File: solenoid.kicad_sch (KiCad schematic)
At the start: 10 parts, among them J9 Solenoid, Q8 DMG3402L

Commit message: Updated schematic. No filtering but besides that finished. Need to fix footprints and start layout.
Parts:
- J9: footprint TerminalBlock:TerminalBlock_bornier-3_P5.08mm -> 0UCIRP-KiCAD-Lib:GX-16 3 pin
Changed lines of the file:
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@@
 			)
 		)
-		(property "Footprint" "TerminalBlock:TerminalBlock_bornier-3_P5.08mm"
+		(property "Footprint" "0UCIRP-KiCAD-Lib:GX-16 3 pin"
 			(at 109.22 83.82 0)
 			(effects

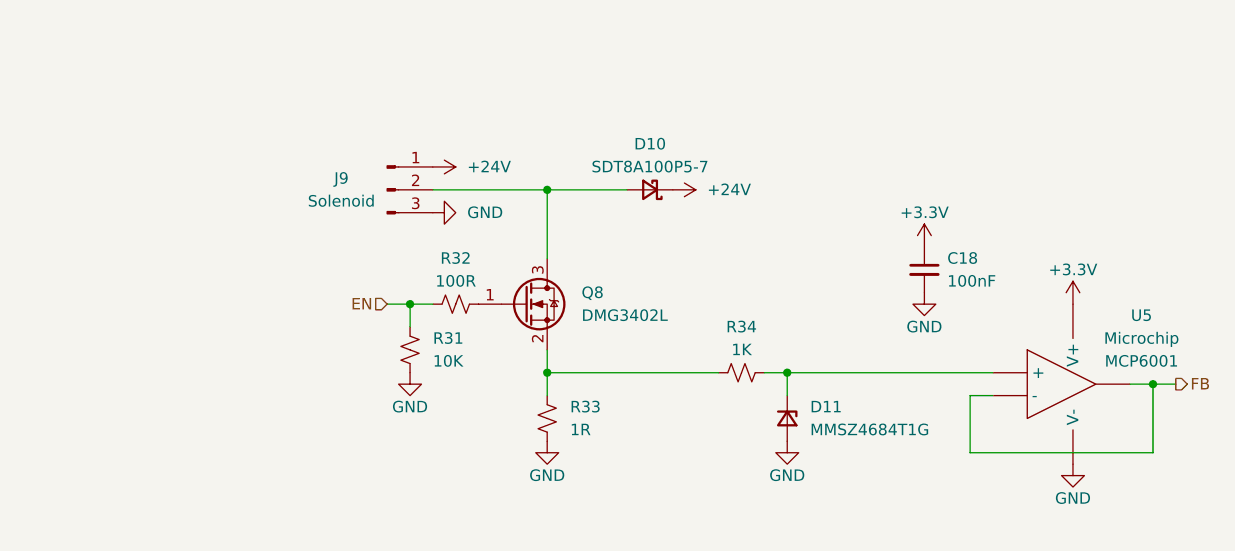
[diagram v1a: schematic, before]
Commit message: Added LC filter for power filtering
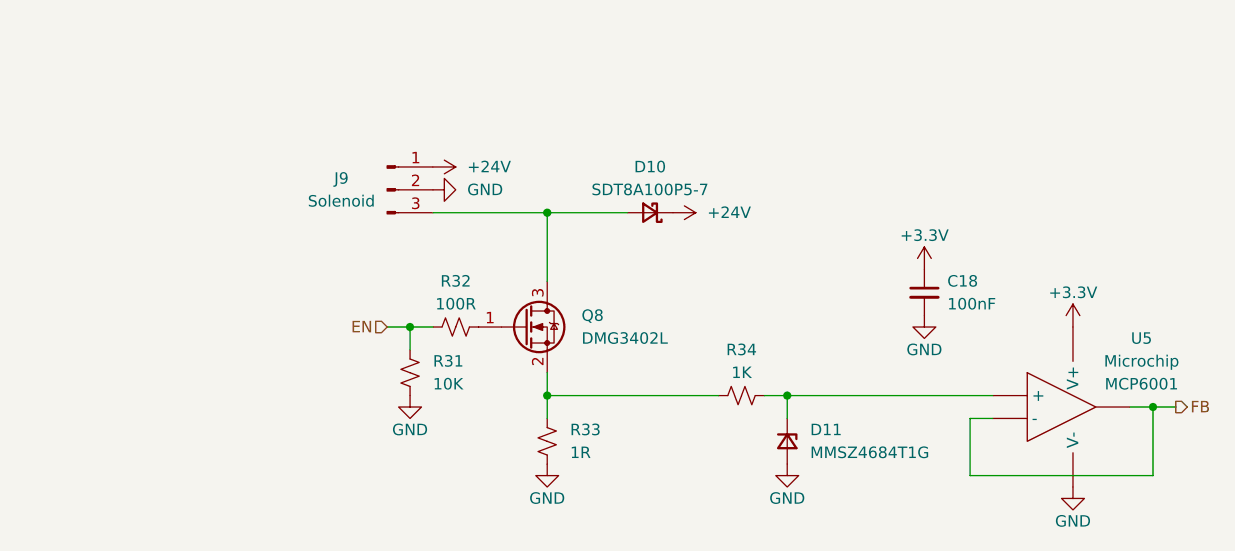
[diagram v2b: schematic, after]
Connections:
- net GND: now also J9.2 (Pin_2); no longer J9.3 (Pin_3)
- net at D10.2 (A), Q8.3 (D): now also J9.3 (Pin_3); no longer J9.2 (Pin_2)
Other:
- moved on the sheet: C18, D10, D11, Q8, R31, R32, R33, R34, U5

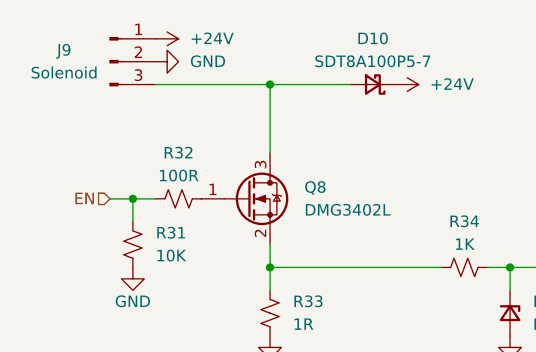
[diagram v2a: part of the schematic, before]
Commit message: Updated kicad lib commit, maybe correct now
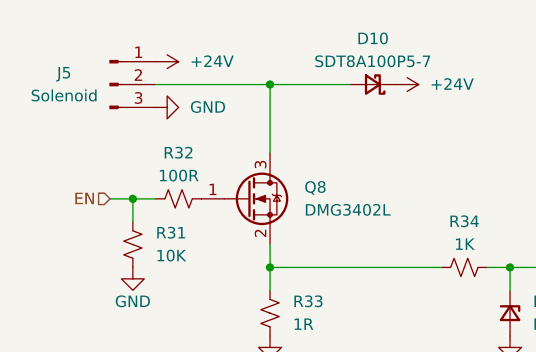
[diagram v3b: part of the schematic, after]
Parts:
- removed J9: Solenoid, 0UCIRP-KiCAD-Lib:GX-16 3 pin, symbol Connector:Conn_01x03_Pin
- added J5: Solenoid, 0UCIRP-KiCAD-Lib:GX-16 3 pin, symbol Connector:Conn_01x03_Pin
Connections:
- net +24V: now also J5.1 (Pin_1)
- net GND: now also J5.3 (Pin_3)
- net at D10.2 (A), Q8.3 (D): now also J5.2 (Pin_2)
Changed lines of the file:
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@@
 	(symbol
 		(lib_id "power:GND")
-		(at 114.3 83.82 90)
+		(at 114.3 88.9 90)
 		(unit 1)
 		(exclude_from_sim no)
@@
 		(fields_autoplaced yes)
 		(property "Reference" "#PWR079"
-			(at 120.65 83.82 0)
+			(at 120.65 88.9 0)
 			(effects
 				(font
@@
 		)
 		(property "Value" "GND"
-			(at 118.11 83.82 90)
+			(at 118.11 88.9 90)
 			(effects
 				(font
@@
 		)
 		(property "Footprint" ""
-			(at 114.3 83.82 0)
+			(at 114.3 88.9 0)
 			(effects
 				(font
@@
 		)
 		(property "Datasheet" ""
-			(at 114.3 83.82 0)
+			(at 114.3 88.9 0)
 			(effects
 				(font
@@
 		)
 		(property "Description" ""
-			(at 114.3 83.82 0)
+			(at 114.3 88.9 0)
 			(effects
 				(font
@@
 			(project "gse2-hardware"
 				(path "/1eb2a3ff-e0fd-4343-8dba-716780a4d459/03932ad1-129b-4688-9d97-fd8248728dfb"
-					(reference "#PWR028")
+					(reference "#PWR0103")
 					(unit 1)
 				)
 				(path "/1eb2a3ff-e0fd-4343-8dba-716780a4d459/286b6f9d-06b9-4eca-96aa-fac563af00a8"
-					(reference "#PWR063")
+					(reference "#PWR0123")
 					(unit 1)
 				)
 				(path "/1eb2a3ff-e0fd-4343-8dba-716780a4d459/3c07b789-4554-4158-a611-d22d74095257"
-					(reference "#PWR0123")
+					(reference "#PWR0429")
 					(unit 1)
 				)
@@
 				)
 				(path "/1eb2a3ff-e0fd-4343-8dba-716780a4d459/4a437018-65cd-45b6-9348-2044032dd86a"
+					(reference "#PWR0427")
+					(unit 1)
+				)
+				(path "/1eb2a3ff-e0fd-4343-8dba-716780a4d459/62945beb-192a-4537-9ce7-3a53d30b8410"
+					(reference "#PWR0421")
+					(unit 1)
+				)
+				(path "/1eb2a3ff-e0fd-4343-8dba-716780a4d459/8a44b462-584f-4ea8-be91-d4caf81deda4"
+					(reference "#PWR0425")
+					(unit 1)
+				)
+				(path "/1eb2a3ff-e0fd-4343-8dba-716780a4d459/94c0f81a-efb8-4875-8214-c5f2a6a703c9"
+					(reference "#PWR0423")
+					(unit 1)
+				)
+				(path "/1eb2a3ff-e0fd-4343-8dba-716780a4d459/dedc65d9-5cd8-484a-8156-18d824848e23"
 					(reference "#PWR0113")
-					(unit 1)
-				)
-				(path "/1eb2a3ff-e0fd-4343-8dba-716780a4d459/62945beb-192a-4537-9ce7-3a53d30b8410"
-					(reference "#PWR073")
-					(unit 1)
-				)
-				(path "/1eb2a3ff-e0fd-4343-8dba-716780a4d459/8a44b462-584f-4ea8-be91-d4caf81deda4"
-					(reference "#PWR0103")
-					(unit 1)
-				)
-				(path "/1eb2a3ff-e0fd-4343-8dba-716780a4d459/94c0f81a-efb8-4875-8214-c5f2a6a703c9"
-					(reference "#PWR093")
-					(unit 1)
-				)
-				(path "/1eb2a3ff-e0fd-4343-8dba-716780a4d459/dedc65d9-5cd8-484a-8156-18d824848e23"
-					(reference "#PWR039")
 					(unit 1)
 				)
@@
 	(symbol
 		(lib_id "power:+24V")
-		(at 114.3 81.28 270)
+		(at 114.3 83.82 270)
 		(unit 1)
 		(exclude_from_sim no)
@@
 		(fields_autoplaced yes)
 		(property "Reference" "#PWR078"
-			(at 110.49 81.28 0)
+			(at 110.49 83.82 0)
 			(effects
 				(font
@@
 		)
 		(property "Value" "+24V"
-			(at 118.11 81.28 90)
+			(at 118.11 83.82 90)
 			(effects
 				(font
@@
 		)
 		(property "Footprint" ""
-			(at 114.3 81.28 0)
+			(at 114.3 83.82 0)
 			(effects
 				(font
@@
 		)
 		(property "Datasheet" ""
-			(at 114.3 81.28 0)
+			(at 114.3 83.82 0)
 			(effects
 				(font
@@
 		)
 		(property "Description" ""
-			(at 114.3 81.28 0)
+			(at 114.3 83.82 0)
 			(effects
 				(font
@@
 			(project "gse2-hardware"
 				(path "/1eb2a3ff-e0fd-4343-8dba-716780a4d459/03932ad1-129b-4688-9d97-fd8248728dfb"
-					(reference "#PWR027")
+					(reference "#PWR0102")
 					(unit 1)
 				)
 				(path "/1eb2a3ff-e0fd-4343-8dba-716780a4d459/286b6f9d-06b9-4eca-96aa-fac563af00a8"
-					(reference "#PWR058")
+					(reference "#PWR0122")
 					(unit 1)
 				)
 				(path "/1eb2a3ff-e0fd-4343-8dba-716780a4d459/3c07b789-4554-4158-a611-d22d74095257"
-					(reference "#PWR0122")
+					(reference "#PWR0428")
 					(unit 1)
 				)
@@
 				)
 				(path "/1eb2a3ff-e0fd-4343-8dba-716780a4d459/4a437018-65cd-45b6-9348-2044032dd86a"
+					(reference "#PWR0426")
+					(unit 1)
+				)
+				(path "/1eb2a3ff-e0fd-4343-8dba-716780a4d459/62945beb-192a-4537-9ce7-3a53d30b8410"
+					(reference "#PWR0420")
+					(unit 1)
+				)
+				(path "/1eb2a3ff-e0fd-4343-8dba-716780a4d459/8a44b462-584f-4ea8-be91-d4caf81deda4"
+					(reference "#PWR0424")
+					(unit 1)
+				)
+				(path "/1eb2a3ff-e0fd-4343-8dba-716780a4d459/94c0f81a-efb8-4875-8214-c5f2a6a703c9"
+					(reference "#PWR0422")
+					(unit 1)
+				)
+				(path "/1eb2a3ff-e0fd-4343-8dba-716780a4d459/dedc65d9-5cd8-484a-8156-18d824848e23"
 					(reference "#PWR0112")
-					(unit 1)
-				)
-				(path "/1eb2a3ff-e0fd-4343-8dba-716780a4d459/62945beb-192a-4537-9ce7-3a53d30b8410"
-					(reference "#PWR072")
-					(unit 1)
-				)
-				(path "/1eb2a3ff-e0fd-4343-8dba-716780a4d459/8a44b462-584f-4ea8-be91-d4caf81deda4"
-					(reference "#PWR0102")
-					(unit 1)
-				)
-				(path "/1eb2a3ff-e0fd-4343-8dba-716780a4d459/94c0f81a-efb8-4875-8214-c5f2a6a703c9"
-					(reference "#PWR092")
-					(unit 1)
-				)
-				(path "/1eb2a3ff-e0fd-4343-8dba-716780a4d459/dedc65d9-5cd8-484a-8156-18d824848e23"
-					(reference "#PWR038")
-					(unit 1)
-				)
-			)
-		)
-	)
-	(symbol
-		(lib_id "Connector:Conn_01x03_Pin")
-		(at 109.22 83.82 0)
-		(unit 1)
-		(exclude_from_sim no)
-		(in_bom yes)
-		(on_board yes)
-		(dnp no)
-		(property "Reference" "J9"
-			(at 104.14 82.55 0)
-			(effects
-				(font
-					(size 1.27 1.27)
-				)
-			)
-		)
-		(property "Value" "Solenoid"
-			(at 104.14 85.09 0)
-			(effects
-				(font
-					(size 1.27 1.27)
-				)
-			)
-		)
-		(property "Footprint" "0UCIRP-KiCAD-Lib:GX-16 3 pin"
-			(at 109.22 83.82 0)
-			(effects
-				(font
-					(size 1.27 1.27)
-				)
-				(hide yes)
-			)
-		)
-		(property "Datasheet" "~"
-			(at 109.22 83.82 0)
-			(effects
-				(font
-					(size 1.27 1.27)
-				)
-				(hide yes)
-			)
-		)
-		(property "Description" ""
-			(at 109.22 83.82 0)
-			(effects
-				(font
-					(size 1.27 1.27)
-				)
-			)
-		)
-		(property "Manufacturer" "~"
-			(at 109.22 83.82 0)
-			(effects
-				(font
-					(size 1.27 1.27)
-				)
-				(hide yes)
-			)
-		)
-		(property "Part #" "~"
-			(at 109.22 83.82 0)
-			(effects
-				(font
-					(size 1.27 1.27)
-				)
-				(hide yes)
-			)
-		)
-		(pin "1"
-		)
-		(pin "2"
-		)
-		(pin "3"
-		)
-		(instances
-			(project "gse2-hardware"
-				(path "/1eb2a3ff-e0fd-4343-8dba-716780a4d459/03932ad1-129b-4688-9d97-fd8248728dfb"
-					(reference "J5")
-					(unit 1)
-				)
-				(path "/1eb2a3ff-e0fd-4343-8dba-716780a4d459/286b6f9d-06b9-4eca-96aa-fac563af00a8"
-					(reference "J7")
-					(unit 1)
-				)
-				(path "/1eb2a3ff-e0fd-4343-8dba-716780a4d459/3c07b789-4554-4158-a611-d22d74095257"
-					(reference "J13")
-					(unit 1)
-				)
-				(path "/1eb2a3ff-e0fd-4343-8dba-716780a4d459/466853be-b1ef-4aae-8a48-67d83205b6e0"
-					(reference "J9")
-					(unit 1)
-				)
-				(path "/1eb2a3ff-e0fd-4343-8dba-716780a4d459/4a437018-65cd-45b6-9348-2044032dd86a"
-					(reference "J12")
-					(unit 1)
-				)
-				(path "/1eb2a3ff-e0fd-4343-8dba-716780a4d459/62945beb-192a-4537-9ce7-3a53d30b8410"
-					(reference "J8")
-					(unit 1)
-				)
-				(path "/1eb2a3ff-e0fd-4343-8dba-716780a4d459/8a44b462-584f-4ea8-be91-d4caf81deda4"
-					(reference "J11")
-					(unit 1)
-				)
-				(path "/1eb2a3ff-e0fd-4343-8dba-716780a4d459/94c0f81a-efb8-4875-8214-c5f2a6a703c9"
-					(reference "J10")
-					(unit 1)
-				)
-				(path "/1eb2a3ff-e0fd-4343-8dba-716780a4d459/dedc65d9-5cd8-484a-8156-18d824848e23"
-					(reference "J6")
 					(unit 1)
 				)
@@
 					(unit 1)
 				)
+			)
+		)
+	)
+	(symbol
+		(lib_id "Connector:Conn_01x03_Pin")
+		(at 109.22 86.36 0)
+		(unit 1)
+		(exclude_from_sim no)
+		(in_bom yes)
+		(on_board yes)
+		(dnp no)
+		(property "Reference" "J5"
+			(at 104.14 85.09 0)
+			(effects
+				(font
+					(size 1.27 1.27)
+				)
+			)
+		)
+		(property "Value" "Solenoid"
+			(at 104.14 87.63 0)
+			(effects
+				(font
+					(size 1.27 1.27)
+				)
+			)
+		)
+		(property "Footprint" "0UCIRP-KiCAD-Lib:GX-16 3 pin"
+			(at 109.22 86.36 0)
+			(effects
+				(font
+					(size 1.27 1.27)
+				)
+				(hide yes)
+			)
+		)
+		(property "Datasheet" "~"
+			(at 109.22 86.36 0)
+			(effects
+				(font
+					(size 1.27 1.27)
+				)
+				(hide yes)
+			)
+		)
+		(property "Description" ""
+			(at 109.22 86.36 0)
+			(effects
+				(font
+					(size 1.27 1.27)
+				)
+			)
+		)
+		(property "Manufacturer" "~"
+			(at 109.22 86.36 0)
+			(effects
+				(font
+					(size 1.27 1.27)
+				)
+				(hide yes)
+			)
+		)
+		(property "Part #" "~"
+			(at 109.22 86.36 0)
+			(effects
+				(font
+					(size 1.27 1.27)
+				)
+				(hide yes)
+			)
+		)
+		(pin "1"
+		)
+		(pin "2"
+		)
+		(pin "3"
+		)
+		(instances
+			(project "gse2-hardware"
+				(path "/1eb2a3ff-e0fd-4343-8dba-716780a4d459/03932ad1-129b-4688-9d97-fd8248728dfb"
+					(reference "J6")
+					(unit 1)
+				)
+				(path "/1eb2a3ff-e0fd-4343-8dba-716780a4d459/286b6f9d-06b9-4eca-96aa-fac563af00a8"
+					(reference "J8")
+					(unit 1)
+				)
+				(path "/1eb2a3ff-e0fd-4343-8dba-716780a4d459/3c07b789-4554-4158-a611-d22d74095257"
+					(reference "J39")
+					(unit 1)
+				)
+				(path "/1eb2a3ff-e0fd-4343-8dba-716780a4d459/466853be-b1ef-4aae-8a48-67d83205b6e0"
+					(reference "J5")
+					(unit 1)
+				)
+				(path "/1eb2a3ff-e0fd-4343-8dba-716780a4d459/4a437018-65cd-45b6-9348-2044032dd86a"
+					(reference "J13")
+					(unit 1)
+				)
+				(path "/1eb2a3ff-e0fd-4343-8dba-716780a4d459/62945beb-192a-4537-9ce7-3a53d30b8410"
+					(reference "J10")
+					(unit 1)
+				)
+				(path "/1eb2a3ff-e0fd-4343-8dba-716780a4d459/8a44b462-584f-4ea8-be91-d4caf81deda4"
+					(reference "J12")
+					(unit 1)
+				)
+				(path "/1eb2a3ff-e0fd-4343-8dba-716780a4d459/94c0f81a-efb8-4875-8214-c5f2a6a703c9"
+					(reference "J11")
+					(unit 1)
+				)
+				(path "/1eb2a3ff-e0fd-4343-8dba-716780a4d459/dedc65d9-5cd8-484a-8156-18d824848e23"
+					(reference "J7")
+					(unit 1)
+				)

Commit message: Subsystem level layout done (prelim)
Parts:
- C18: footprint Capacitor_SMD:C_0402_1005Metric -> Capacitor_SMD:C_0603_1608Metric
- R31, R32, R34: footprint Resistor_SMD:R_0402_1005Metric -> Resistor_SMD:R_0603_1608Metric
- R33: footprint Resistor_SMD:R_2512_6332Metric -> Resistor_SMD:R_0603_1608Metric
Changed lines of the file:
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@@
 			)
 		)
-		(property "Footprint" "Resistor_SMD:R_2512_6332Metric"
+		(property "Footprint" "Resistor_SMD:R_0603_1608Metric"
 			(at 127 111.76 0)
 			(effects
@@
 			)
 		)
-		(property "Footprint" "Capacitor_SMD:C_0402_1005Metric"
+		(property "Footprint" "Capacitor_SMD:C_0603_1608Metric"
 			(at 168.91 95.25 0)
 			(effects
@@
 			)
 		)
-		(property "Footprint" "Resistor_SMD:R_0402_1005Metric"
+		(property "Footprint" "Resistor_SMD:R_0603_1608Metric"
 			(at 111.76 104.14 0)
 			(effects
@@
 			)
 		)
-		(property "Footprint" "Resistor_SMD:R_0402_1005Metric"
+		(property "Footprint" "Resistor_SMD:R_0603_1608Metric"
 			(at 148.59 106.68 0)
 			(effects
@@
 			)
 		)
-		(property "Footprint" "Resistor_SMD:R_0402_1005Metric"
+		(property "Footprint" "Resistor_SMD:R_0603_1608Metric"
 			(at 116.84 99.06 0)
 			(effects

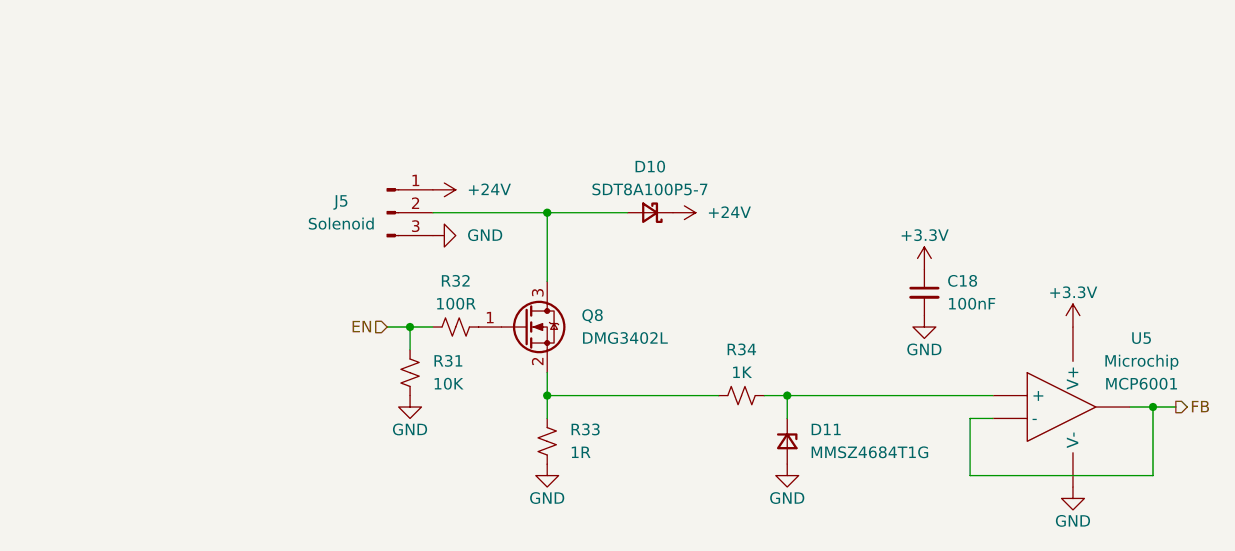
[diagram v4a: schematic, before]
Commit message: GSE v2.1: Updates for DSUB connectors for schematic only done. Layout needs a ton of work
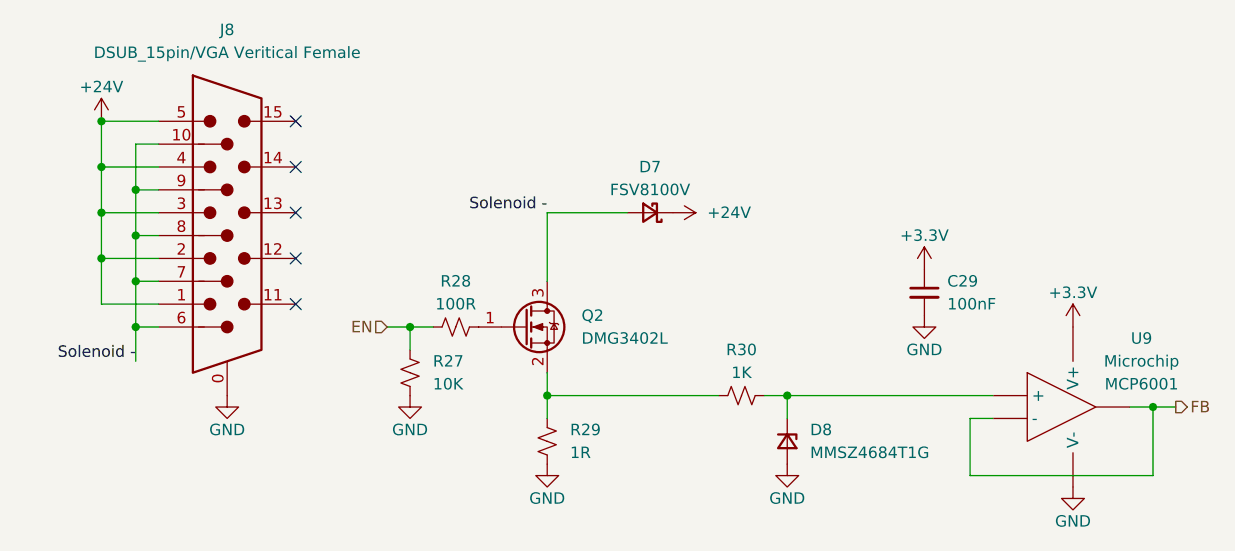
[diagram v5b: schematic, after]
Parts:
- removed J5: Solenoid, 0UCIRP-KiCAD-Lib:GX-16 3 pin, symbol Connector:Conn_01x03_Pin
- added J8: DSUB_15pin/VGA Veritical Female, 0UCIRP-KiCAD-Lib:Connector_VGA_Vertical, symbol 0UCIRP-KiCAD-Lib:Connector_VGA_vertical
- D7: renamed from D10; value SDT8A100P5-7 -> FSV8100V
- U9: renamed from U5; value ~ -> MCP6001
- renumbered C18 to C29, D11 to D8, Q8 to Q2, R31 to R27, R32 to R28, R33 to R29, R34 to R30
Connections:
- net +24V: now also J8.1, J8.2, J8.3, J8.4, J8.5
- net GND: now also J8.0
- net Solenoid -: now reaches D7.2 (A), Q2.3 (D)
- net Solenoid -: now also J8.10, J8.6, J8.7, J8.8, J8.9
- no-connect marks 0 -> 5

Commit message: GSE v2.1 done, just waiting on prop rn to finalize their sensor list
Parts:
- removed U9: MCP6001, Package_TO_SOT_SMD:SOT-23-5, symbol UCIRP-KiCAD-Lib:MCP6001
- added U9: MCP6001, 0UCIRP-KiCAD-Lib:Op-amp MCP6001, symbol 0UCIRP-KiCAD-Lib:Op-amp MCP6001
- D7: footprint Diode_SMD:D_PowerDI-5 -> 0UCIRP-KiCAD-Lib:Diode_Schottky (100V_80A) FSV8100V; Manufacturer Diodes -> (none); Part # SDT8A100P5-7 -> FSV8100V
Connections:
- net +3.3V: now also U9.5 (V+)
- net FB: now also U9.1, U9.4 (-)
- net GND: now also U9.2 (V-)
- net at D8.1 (K), R30.2: now also U9.3 (+)

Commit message: GSE v2.1: small changes made and typos
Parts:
- J8: value DSUB_15pin/VGA Veritical Female -> DSUB_15pin/VGA Vertical Female
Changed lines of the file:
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@@
 			)
 		)
-		(property "Value" "DSUB_15pin/VGA Veritical  Female"
+		(property "Value" "DSUB_15pin/VGA Vertical  Female"
 			(at 91.44 68.58 0)
 			(effects

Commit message: GSE v2.1: Done, ready for JLCPCB
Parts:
- renumbered D7 to D10, D8 to D11, R27 to R30, R28 to R31, R29 to R32, R30 to R33
